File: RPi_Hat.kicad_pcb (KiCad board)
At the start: 2 copper layers, 65 x 56 mm, 5 parts, among them J2 RPi_GPIO

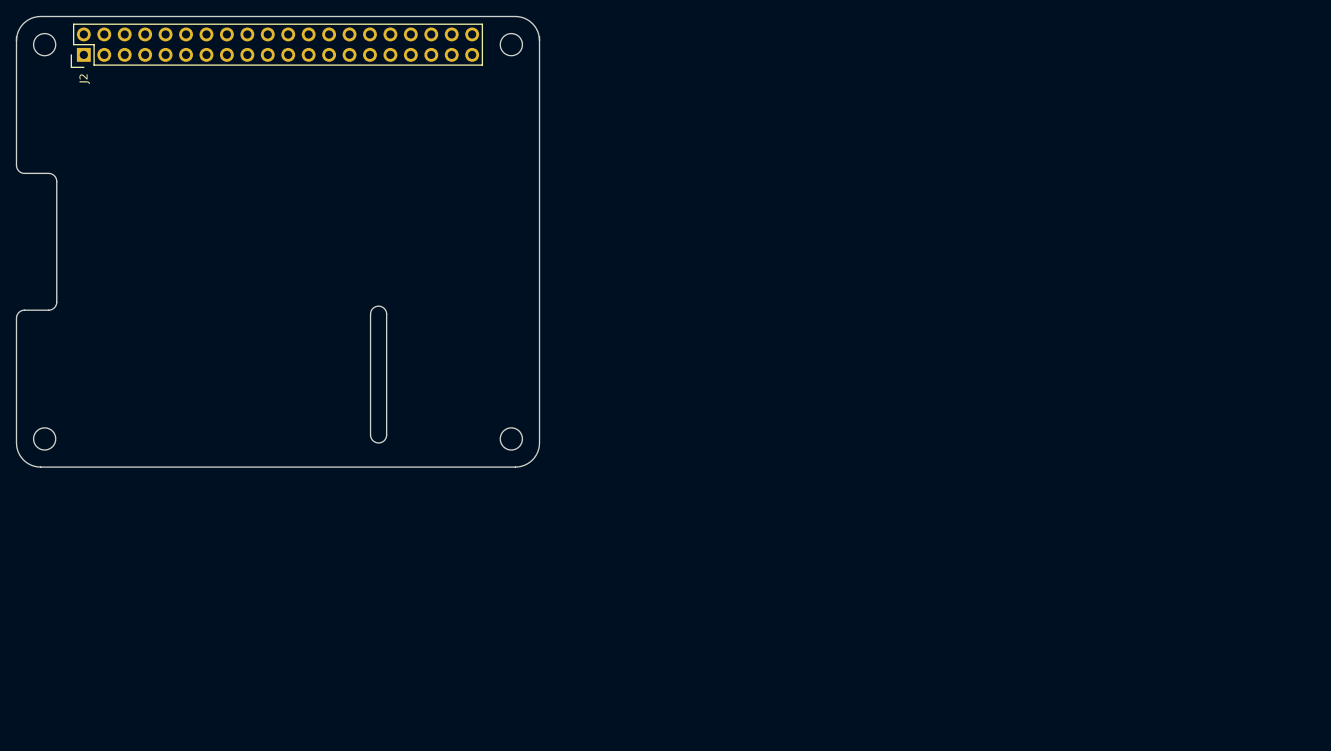
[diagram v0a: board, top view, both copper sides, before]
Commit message: Finish schem and start routing
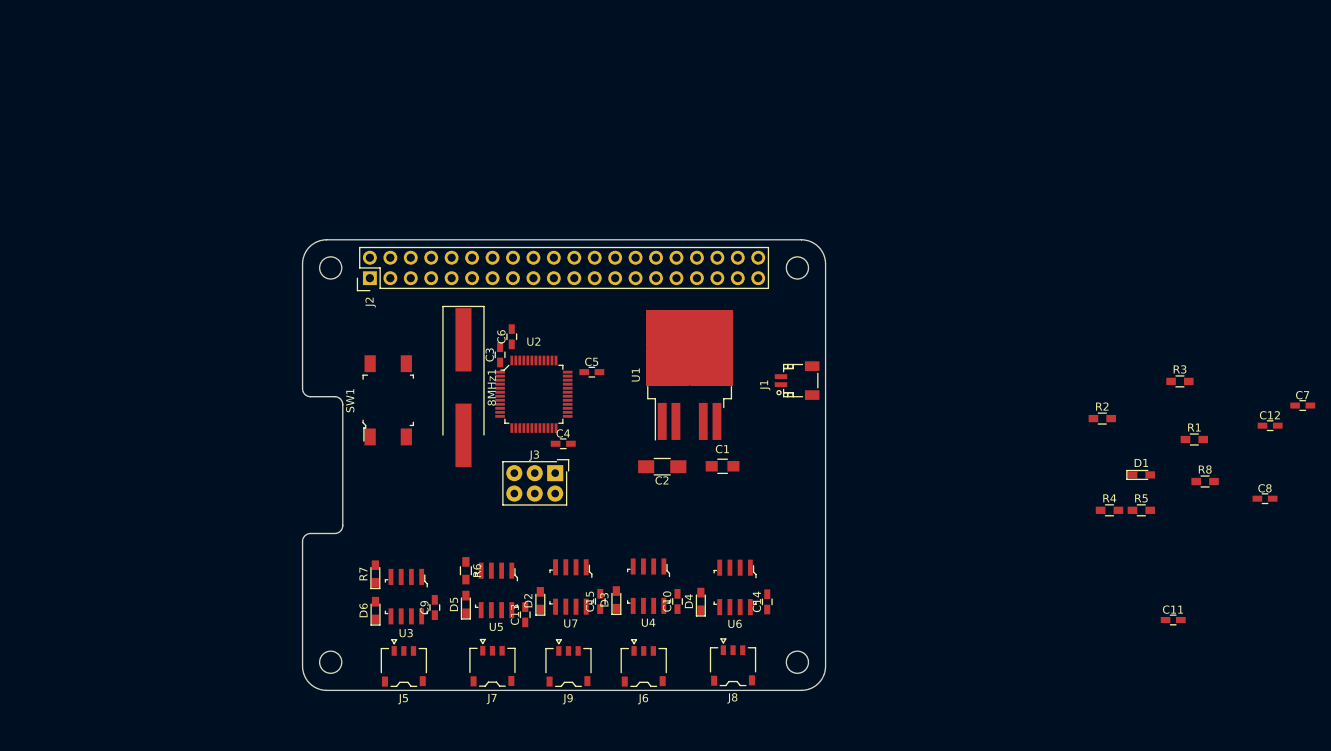
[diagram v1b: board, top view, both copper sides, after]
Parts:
- added 8MHz1: Crystal, Crystals:Crystal_SMD_HC49-SD_HandSoldering, F.Cu at (55.5, 46.6)
- added C1: 10uF, Inductors_SMD:L_0805_HandSoldering, F.Cu at (87.8, 56.4)
- added C10: 0.1uF, Capacitors_SMD:C_0603_HandSoldering, F.Cu at (82.2, 73.2)
- added C11: 20pF, Capacitors_SMD:C_0603_HandSoldering, F.Cu at (143.8, 75.5)
- added C12: 20pF, Capacitors_SMD:C_0603_HandSoldering, F.Cu at (155.8, 51.4)
- added C13: 0.1uF, Capacitors_SMD:C_0603_HandSoldering, F.Cu at (63.2, 74.8)
- added C14: 0.1uF, Capacitors_SMD:C_0603_HandSoldering, F.Cu at (93.3, 73.2)
- added C15: 0.1uF, Capacitors_SMD:C_0603_HandSoldering, F.Cu at (72.5, 73.2)
- added C2: 100uF, Capacitors_SMD:C_1206_HandSoldering, F.Cu at (80.2, 56.5)
- added C3: 0.1uF, Capacitors_SMD:C_0603_HandSoldering, F.Cu at (60.1, 42.5)
- added C4: 0.1uF, Capacitors_SMD:C_0603_HandSoldering, F.Cu at (68.0, 53.6)
- added C5: 0.1uF, Capacitors_SMD:C_0603_HandSoldering, F.Cu at (71.5, 44.7)
- added C6: 0.1uF, Capacitors_SMD:C_0603_HandSoldering, F.Cu at (61.5, 40.3)
- added C7: 0.1uF, Capacitors_SMD:C_0603_HandSoldering, F.Cu at (159.8, 48.9)
- added C8: 0.1uF, Capacitors_SMD:C_0603_HandSoldering, F.Cu at (155.2, 60.4)
- added C9: 0.1uF, Capacitors_SMD:C_0603_HandSoldering, F.Cu at (52.0, 74.0)
- added D1: LED, LEDs:LED_0603_HandSoldering, F.Cu at (139.8, 57.5)
- added D2: LED, LEDs:LED_0603_HandSoldering, F.Cu at (65.1, 73.1)
- added D3: LED, LEDs:LED_0603_HandSoldering, F.Cu at (74.5, 73.0)
- added D4: LED, LEDs:LED_0603_HandSoldering, F.Cu at (85.0, 73.2)
- added D5: LED, LEDs:LED_0603_HandSoldering, F.Cu at (55.9, 73.6)
- added D6: LED, LEDs:LED_0603_HandSoldering, F.Cu at (44.6, 74.3)
- added J1: Conn_01x02_Male, Connectors_JST:JST_SH_SM02B-SRSS-TB_02x1.00mm_Angled, F.Cu at (97.0, 45.8)
- added J3: Conn_02x03_Counter_Clockwise, Connectors_Samtec:SDL-106-X-XX_2x03, F.Cu at (67.0, 57.2)
- added J5: Conn_01x03_Male, Connectors_JST:JST_ACH_BM03B-ACHSS_03x1.20mm_Angled, F.Cu at (48.1, 81.2)
- added J6: Conn_01x03_Male, Connectors_JST:JST_ACH_BM03B-ACHSS_03x1.20mm_Angled, F.Cu at (78.0, 81.2)
- added J7: Conn_01x03_Male, Connectors_JST:JST_ACH_BM03B-ACHSS_03x1.20mm_Angled, F.Cu at (59.1, 81.2)
- added J8: Conn_01x03_Male, Connectors_JST:JST_ACH_BM03B-ACHSS_03x1.20mm_Angled, F.Cu at (89.0, 81.2)
- added J9: Conn_01x03_Male, Connectors_JST:JST_ACH_BM03B-ACHSS_03x1.20mm_Angled, F.Cu at (68.6, 81.2)
- added R1: 180R, Resistors_SMD:R_0603_HandSoldering, F.Cu at (146.4, 53.1)
- added R2: 180R, Resistors_SMD:R_0603_HandSoldering, F.Cu at (134.9, 50.5)
- added R3: 180R, Resistors_SMD:R_0603_HandSoldering, F.Cu at (144.6, 45.9)
- added R4: 10k, Resistors_SMD:R_0603_HandSoldering, F.Cu at (135.8, 61.9)
- added R5: 180R, Resistors_SMD:R_0603_HandSoldering, F.Cu at (139.8, 61.9)
- added R6: 180R, Resistors_SMD:R_0603_HandSoldering, F.Cu at (55.9, 69.4)
- added R7: 180R, LEDs:LED_0603_HandSoldering, F.Cu at (44.6, 69.8)
- added R8: 10k, Resistors_SMD:R_0603_HandSoldering, F.Cu at (147.7, 58.3)
- added SW1: SW_Push, digikey-footprints:Switch_Tactile_SMD_6x6mm, F.Cu at (46.2, 48.2)
- added U1: LM1085-5.0, TO_SOT_Packages_SMD:TO-263-4, F.Cu at (83.7, 45.0)
- added U2: STM32F030CCTx, digikey-footprints:LQFP-48_7x7mm, F.Cu at (64.3, 47.5)
- added U3: MAX485E, digikey-footprints:SOIC-8_W3.9mm, F.Cu at (48.4, 72.6)
- added U4: MAX485E, digikey-footprints:SOIC-8_W3.9mm, F.Cu at (78.5, 71.3)
- added U5: MAX485E, digikey-footprints:SOIC-8_W3.9mm, F.Cu at (59.6, 71.8)
- added U6: MAX485E, digikey-footprints:SOIC-8_W3.9mm, F.Cu at (89.3, 71.5)
- added U7: MAX485E, digikey-footprints:SOIC-8_W3.9mm, F.Cu at (68.9, 71.4)
- moved ? 45.1 mm to (97.0, 31.8)
- moved ? 45.1 mm to (97.0, 80.8)
- moved ? 45.1 mm to (39.0, 80.8)
- moved ? 45.1 mm to (39.0, 31.8)
- moved J2 45.1 mm to (68.0, 31.8)
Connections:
- J2 pad 1: Net-(J2-Pad1) -> +3V3
- J2 pad 14: Net-(J2-Pad14) -> GND
- J2 pad 19: Net-(J2-Pad19) -> /RPi_GPIO/MOSI
- J2 pad 2: Net-(J2-Pad2) -> +5V
- J2 pad 20: Net-(J2-Pad20) -> GND
- J2 pad 21: Net-(J2-Pad21) -> /RPi_GPIO/MISO
- J2 pad 23: Net-(J2-Pad23) -> /RPi_GPIO/SCLK
- J2 pad 25: Net-(J2-Pad25) -> GND
- J2 pad 30: Net-(J2-Pad30) -> GND
- J2 pad 34: Net-(J2-Pad34) -> GND
- J2 pad 39: Net-(J2-Pad39) -> GND
- J2 pad 4: Net-(J2-Pad4) -> +5V
- J2 pad 6: Net-(J2-Pad6) -> GND
- J2 pad 9: Net-(J2-Pad9) -> GND
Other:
- outline, holes or cut-outs redrawn
- board text removed: "Camera Flex Slot (Optional)"
- board text removed: "Dimensions taken from https://github.com/raspberrypi/hats/blob/master/hat-board-mechanical.pdf"
- board text removed: "Select one of these board edges depending upon the type of socket that is used."

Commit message: Place all components on board
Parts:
- moved C8 111.9 mm to (44.9, 41.0)
- moved C12 104.5 mm to (51.3, 53.4), turned to 90 degrees
- moved C7 101.3 mm to (58.6, 49.7), turned to 90 degrees
- moved C11 99.0 mm to (51.5, 39.6), turned to 270 degrees
- moved R4 93.6 mm to (45.1, 39.1), turned to 180 degrees
- moved R8 86.2 mm to (63.5, 39.9), turned to 90 degrees
- moved R3 73.7 mm to (74.5, 68.7), turned to 270 degrees
- moved R2 72.3 mm to (65.0, 68.9), turned to 90 degrees
- moved R5 55.1 mm to (85.1, 68.8), turned to 270 degrees
- moved R1 52.2 mm to (94.2, 54.9), turned to 90 degrees
- moved D1 41.9 mm to (98.0, 54.9), turned to 90 degrees

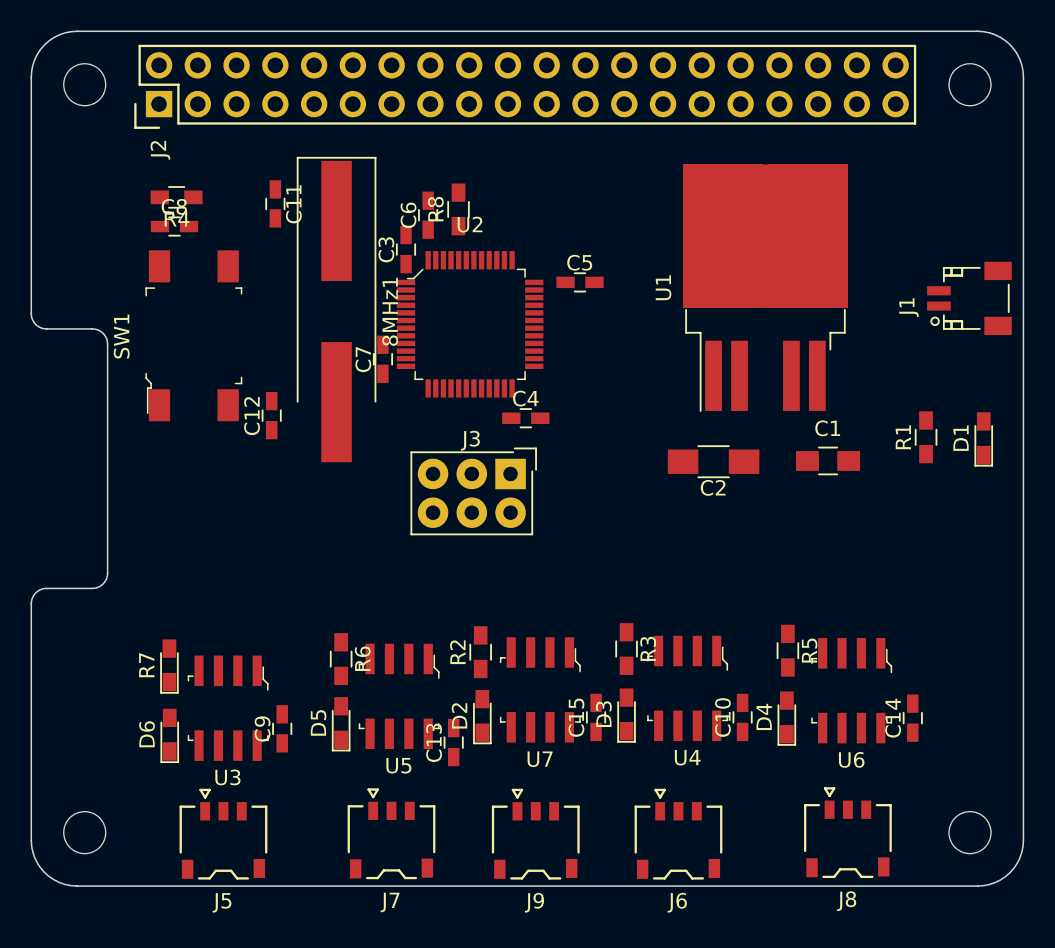
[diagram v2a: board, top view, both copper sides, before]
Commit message: Update footprints, fix gnd missing, start to align connectors
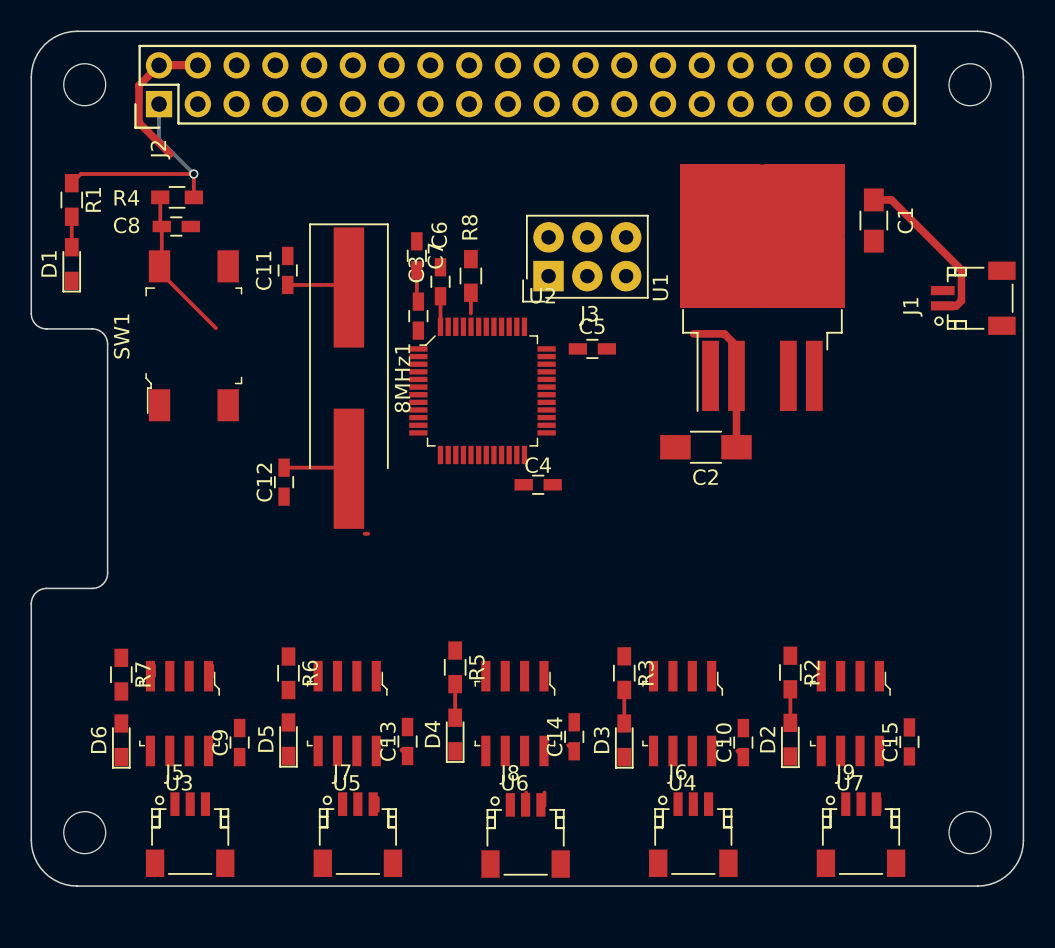
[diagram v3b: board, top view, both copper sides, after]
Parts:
- J5, J6, J7, J8, J9: footprint Connectors_JST:JST_ACH_BM03B-ACHSS_03x1.20mm_Angled -> Connectors_JST:JST_SH_SM03B-SRSS-TB_03x1.00mm_Angled
- R7: footprint LEDs:LED_0603_HandSoldering -> Resistors_SMD:R_0603_HandSoldering
- moved D1 60.8 mm to (38.2, 43.5)
- moved R1 58.1 mm to (38.2, 39.3), turned to 270 degrees
- moved C14 22.2 mm to (71.1, 74.5)
- moved U6 22.1 mm to (67.2, 73.0)
- moved R5 21.8 mm to (63.3, 69.9)
- moved D4 21.8 mm to (63.3, 74.3)
- moved J9 21.3 mm to (89.9, 80.8)
- moved J8 21.1 mm to (67.9, 80.9)
- moved C15 20.6 mm to (93.1, 74.8)
- moved U7 20.4 mm to (89.2, 73.0)
- moved R2 20.3 mm to (85.3, 70.3), turned to 270 degrees
- moved D2 20.2 mm to (85.3, 74.7)
- moved C1 16.0 mm to (90.8, 40.6), turned to 270 degrees
- moved J3 13.2 mm to (69.4, 44.3), turned to 90 degrees
- moved C7 7.13 mm to (60.8, 43.0), turned to 270 degrees
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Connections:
- C3 pad 2: Net-(C3-Pad2) -> GND
- C4 pad 2: Net-(C3-Pad2) -> GND
- C5 pad 2: Net-(C3-Pad2) -> GND
- C6 pad 2: Net-(C3-Pad2) -> GND
- C7 pad 2: Net-(C3-Pad2) -> GND
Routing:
- net +5V: track 0.00 -> 22.0 mm
- net +3V3: track 0.00 -> 19.5 mm, vias 0 -> 1
- net Net-(C1-Pad1): track 0.00 -> 11.0 mm
- net /RPi_GPIO/RESET: track 0.00 -> 10.2 mm
- net /RPi_GPIO/OSC_IN: track 0.00 -> 7.02 mm
- net /RPi_GPIO/OSC_OUT: track 0.00 -> 4.28 mm
- net GND: track 0.00 -> 2.32 mm
- net Net-(D4-Pad2): track 0.00 -> 2.20 mm
- net Net-(D2-Pad2): track 0.00 -> 2.20 mm
- net Net-(D3-Pad2): track 0.00 -> 2.20 mm
- net Net-(D1-Pad2): track 0.00 -> 2.00 mm
- net /RPi_GPIO/BOOT0: track 0.00 -> 1.36 mm
- net /RPi_GPIO/USART4_TX: track 0.00 -> 0.93 mm
- net Net-(J9-Pad3): track 0.00 -> 0.85 mm
- net Net-(J9-Pad2): track 0.00 -> 0.85 mm
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
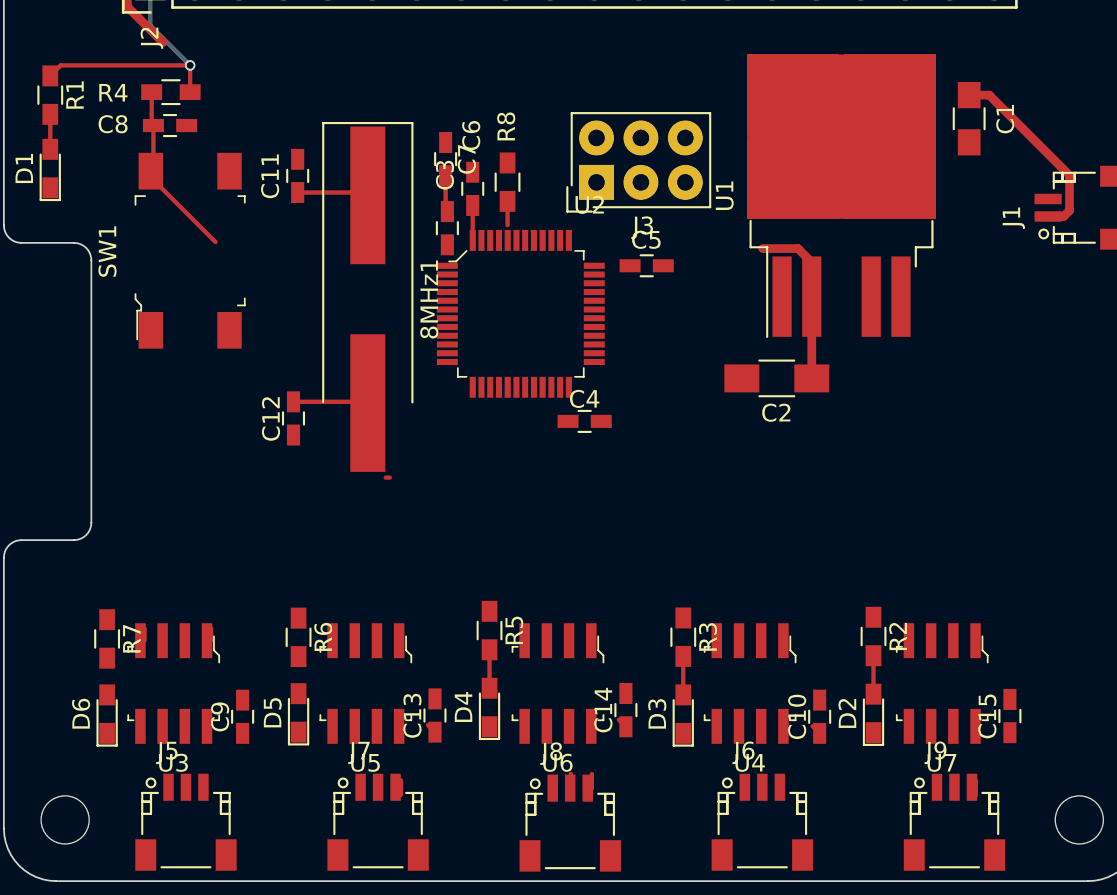
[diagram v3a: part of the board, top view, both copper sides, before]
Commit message: Keepon routing
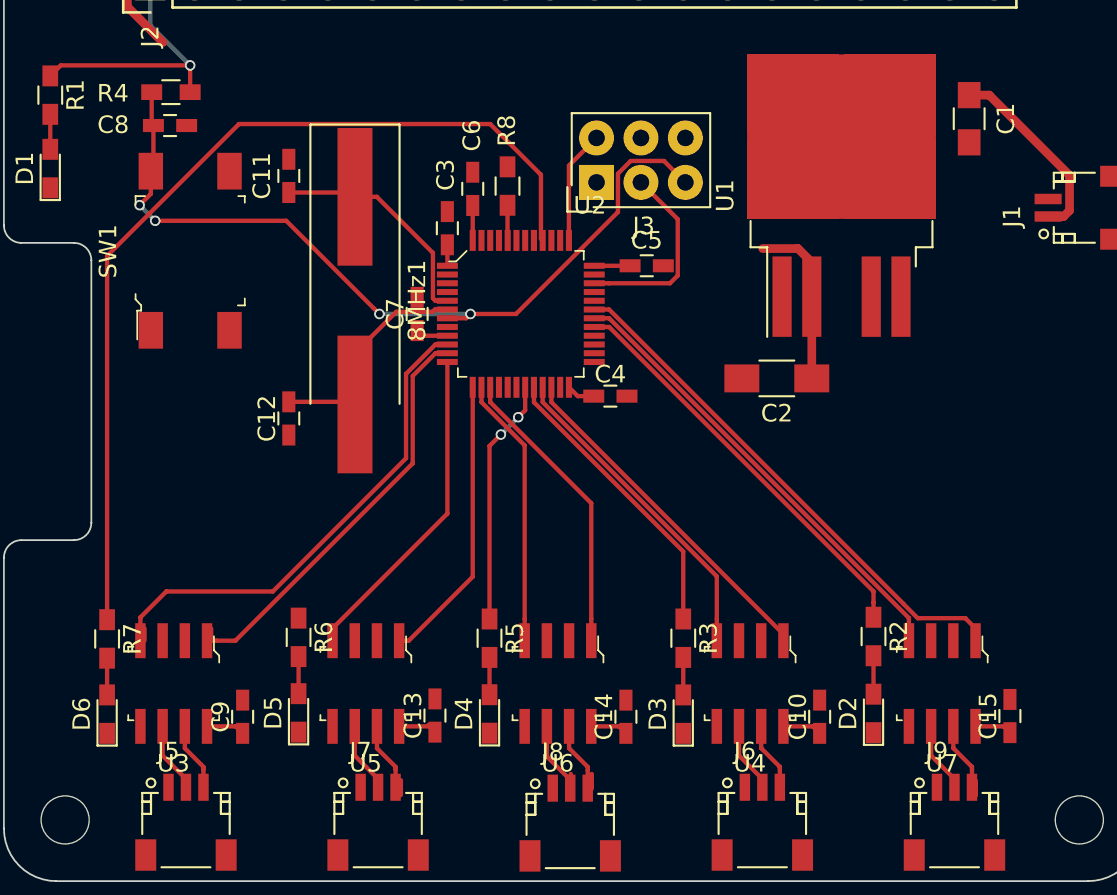
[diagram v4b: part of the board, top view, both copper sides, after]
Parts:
- moved C7 9.00 mm to (59.2, 51.8), turned to 90 degrees
- moved C4 2.06 mm to (70.2, 56.5)
- moved 8MHz1 0.74 mm to (55.6, 51.1)
- moved C11 0.51 mm to (51.8, 43.9)
- moved R5 0.44 mm to (63.3, 70.4)
- moved C14 0.38 mm to (71.1, 74.8)
- moved D4 0.37 mm to (63.3, 74.7)
- moved C12 0.27 mm to (51.8, 57.8)
- moved R8 0.22 mm to (64.3, 44.5)
- moved R3 0.06 mm to (74.4, 70.4)
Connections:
- R2 pad 1: /RPi_GPIO/PB0 -> /RPi_GPIO/PA8
- R3 pad 1: /RPi_GPIO/PB1 -> /RPi_GPIO/PB2
- R5 pad 1: /RPi_GPIO/PB2 -> /RPi_GPIO/PB1
- U2 pad 18: /RPi_GPIO/PB0 -> Net-(U2-Pad18)
- U2 pad 29: Net-(U2-Pad29) -> /RPi_GPIO/PA8
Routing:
- net /RPi_GPIO/PB4: track 0.00 -> 53.7 mm
- net /RPi_GPIO/RESET: track 10.2 -> 47.8 mm, vias 0 -> 4
- net /RPi_GPIO/USART1_RX: track 0.00 -> 30.1 mm
- net /RPi_GPIO/USART4_TX: track 0.93 -> 28.9 mm
- net /RPi_GPIO/USART1_TX: track 0.00 -> 26.4 mm
- net /RPi_GPIO/PA8: track 0.00 -> 23.7 mm
- net /RPi_GPIO/USART4_RX: track 0.70 -> 24.2 mm
- net /RPi_GPIO/USART3_RX: track 0.00 -> 20.0 mm
- net /RPi_GPIO/USART2_TX: track 0.00 -> 18.7 mm
- net /RPi_GPIO/USART3_TX: track 0.00 -> 18.6 mm
- net /RPi_GPIO/USART6_RX: track 0.00 -> 16.9 mm
- net /RPi_GPIO/PB2: track 0.00 -> 16.8 mm
- net /RPi_GPIO/USART2_RX: track 0.00 -> 16.6 mm
- net +3V3: track 19.5 -> 35.7 mm
- net /RPi_GPIO/USART6_TX: track 0.00 -> 15.5 mm
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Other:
- net class Default: clearance 0.2 -> 0.1; trace_width 0.25 -> 0.1
- rule trace_clearance: 0.2 -> 0.1
- rule trace_min: 0.01 -> 0.1

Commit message: Finished routing
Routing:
- net +3V3: track 35.7 -> 189.0 mm, vias 1 -> 7
- net +5V: track 22.0 -> 75.4 mm
- net /RPi_GPIO/PB3: track 0.00 -> 33.3 mm, vias 0 -> 5
- net /RPi_GPIO/MOSI: track 0.00 -> 31.0 mm, vias 0 -> 2
- net /RPi_GPIO/SCLK: track 0.00 -> 30.7 mm, vias 0 -> 2
- net /RPi_GPIO/MISO: track 0.00 -> 30.5 mm, vias 0 -> 2
- net GND: track 0.37 -> 10.7 mm, vias 0 -> 183
- net Net-(C1-Pad1): track 11.0 -> 19.3 mm
- net Net-(J7-Pad3): track 4.77 -> 3.92 mm
- added copper zone on B.Cu, net GND
- added copper zone on F.Cu, net GND
